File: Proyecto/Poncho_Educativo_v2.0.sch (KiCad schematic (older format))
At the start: 0 parts

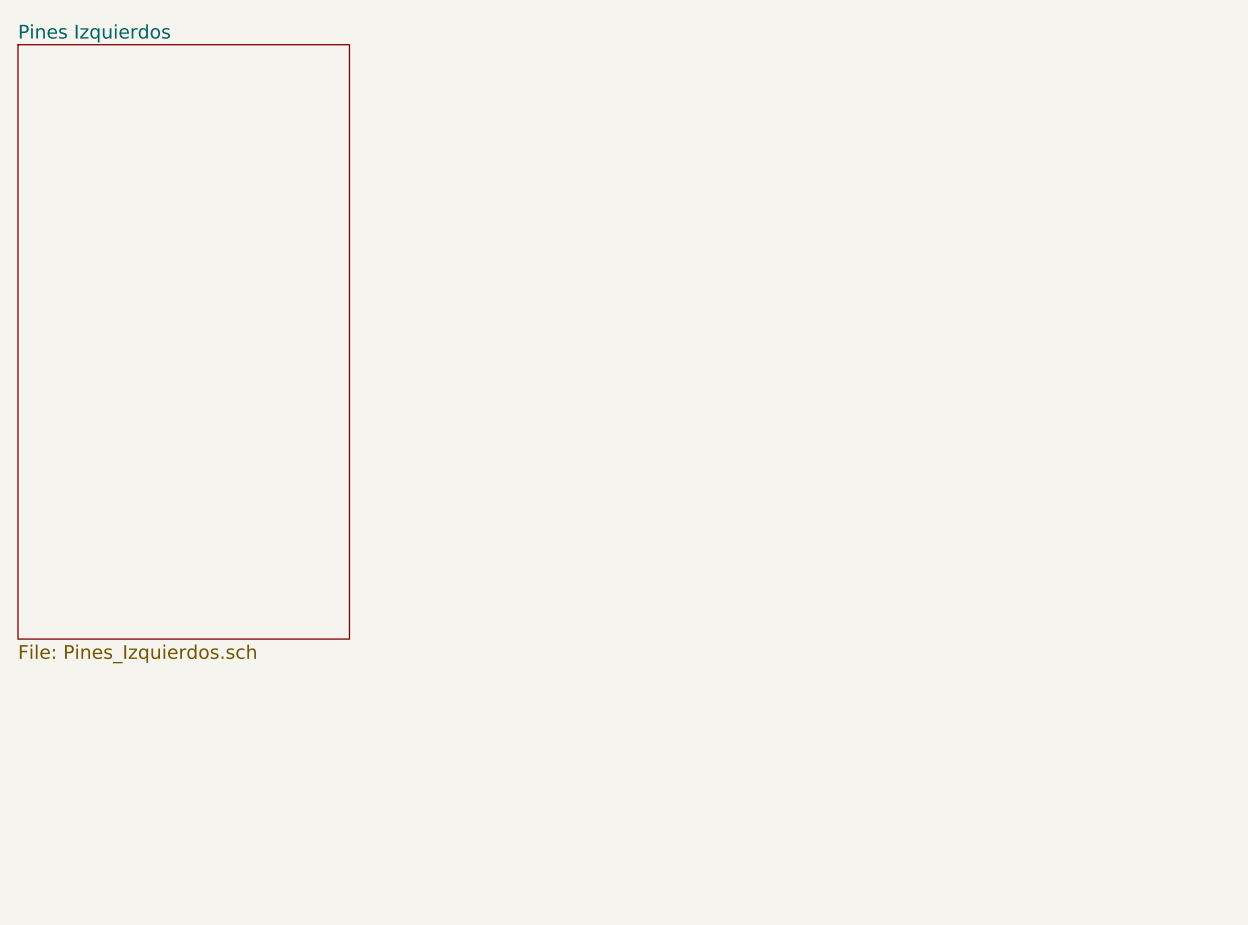
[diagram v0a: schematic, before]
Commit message: Actualización de documentación y esquemáticos.
Se actualizaron los archivos de datos y caracteristicas de los displays
y se adelantó a un 90% el diseño de los esquemáticos de KiCad.
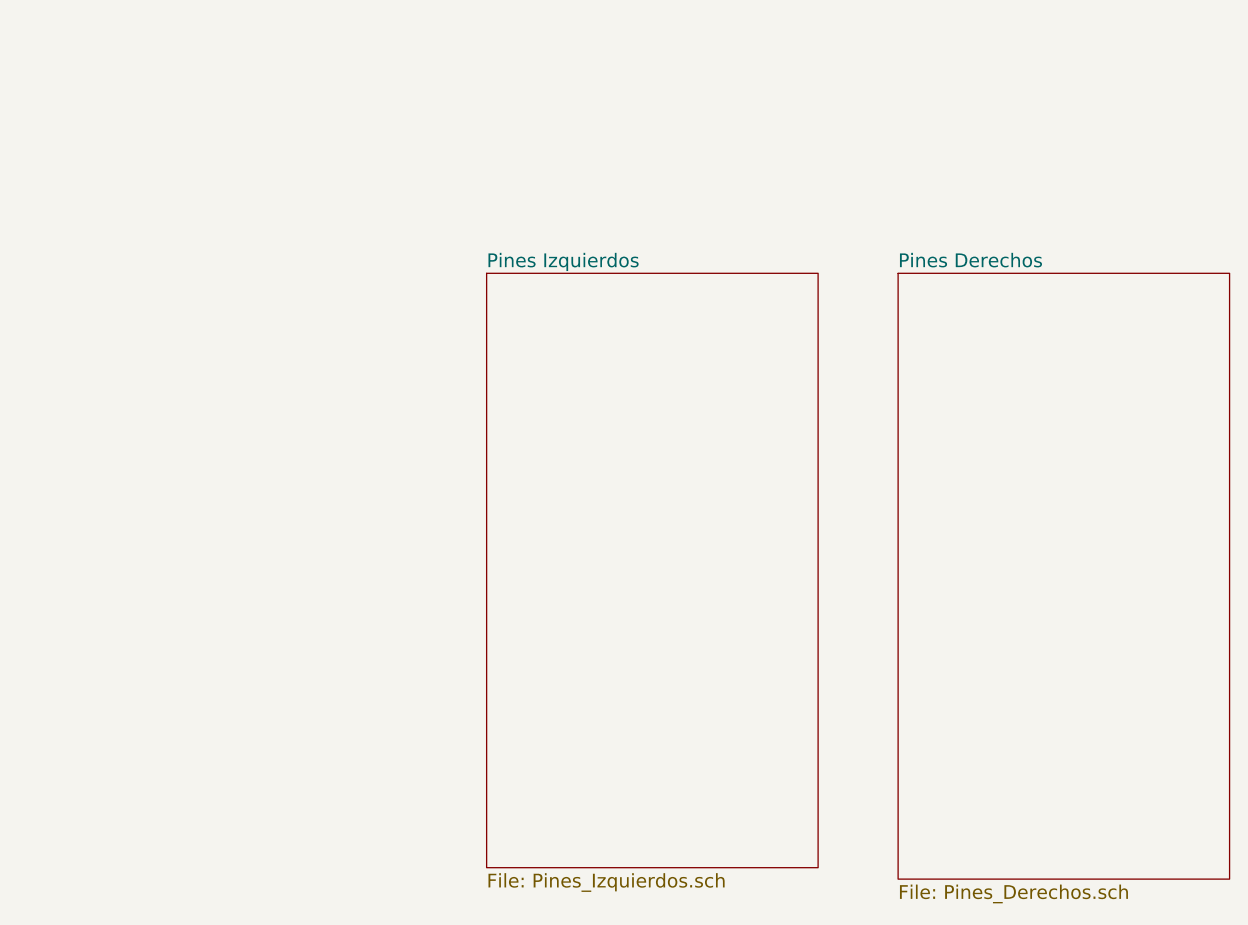
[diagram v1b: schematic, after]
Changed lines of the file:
@@
 EESchema Schematic File Version 2
+LIBS:8x8led-cache
 LIBS:power
 LIBS:device
 LIBS:display
+LIBS:Poncho_Esqueleto
+LIBS:MAX7219
 LIBS:Poncho_Educativo_v2.0-cache
 EELAYER 25 0
@@
 $Descr A4 11693 8268
 encoding utf-8
-Sheet 1 2
+Sheet 1 3
 Title "Poncho Educativo v2.0"
 Date "2017-05-15"
@@
 $EndDescr
 $Sheet
-S 1250 1150 1450 2600
+S 3300 2150 1450 2600
 U 591BB8C8
 F0 "Pines Izquierdos" 60
 F1 "Pines_Izquierdos.sch" 60
 $EndSheet
+$Sheet
+S 5100 2150 1450 2650
+U 5926FB74
+F0 "Pines Derechos" 60
+F1 "Pines_Derechos.sch" 60
+$EndSheet
 $EndSCHEMATC

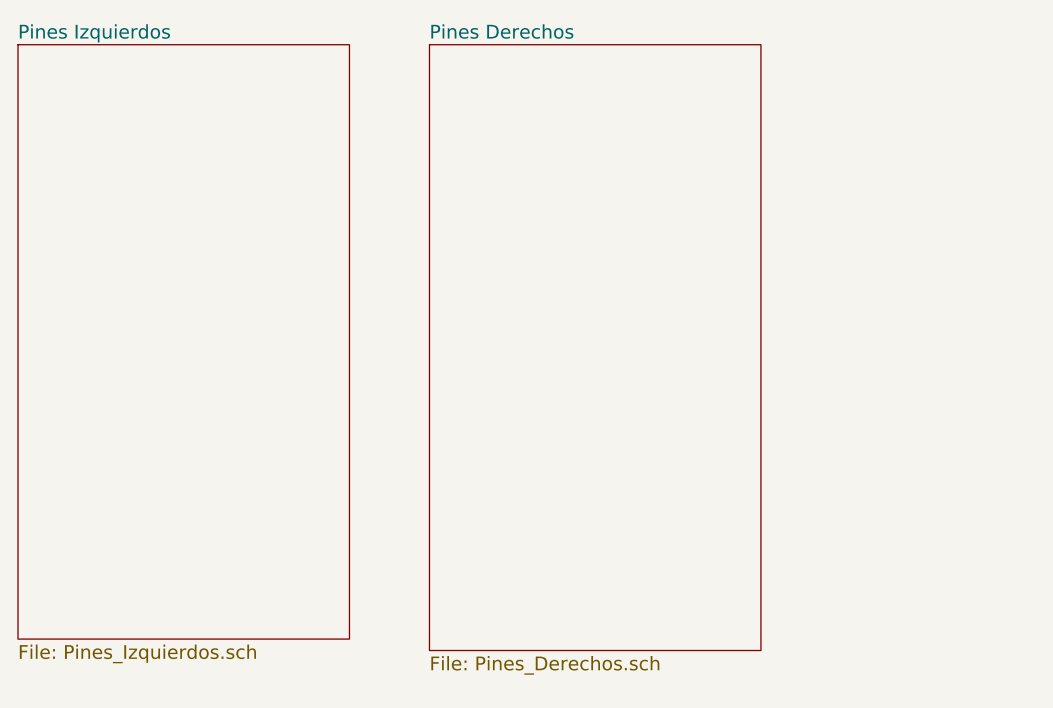
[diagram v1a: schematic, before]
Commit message: Avance de FootPrints
Se terminó diseño de esquemáticos en ojas Jerárquicas; se avanzó a un
70% en las referencias de FootPrint, y se actualizaron hojas de datos de
la Matriz de LEDs 8x8.
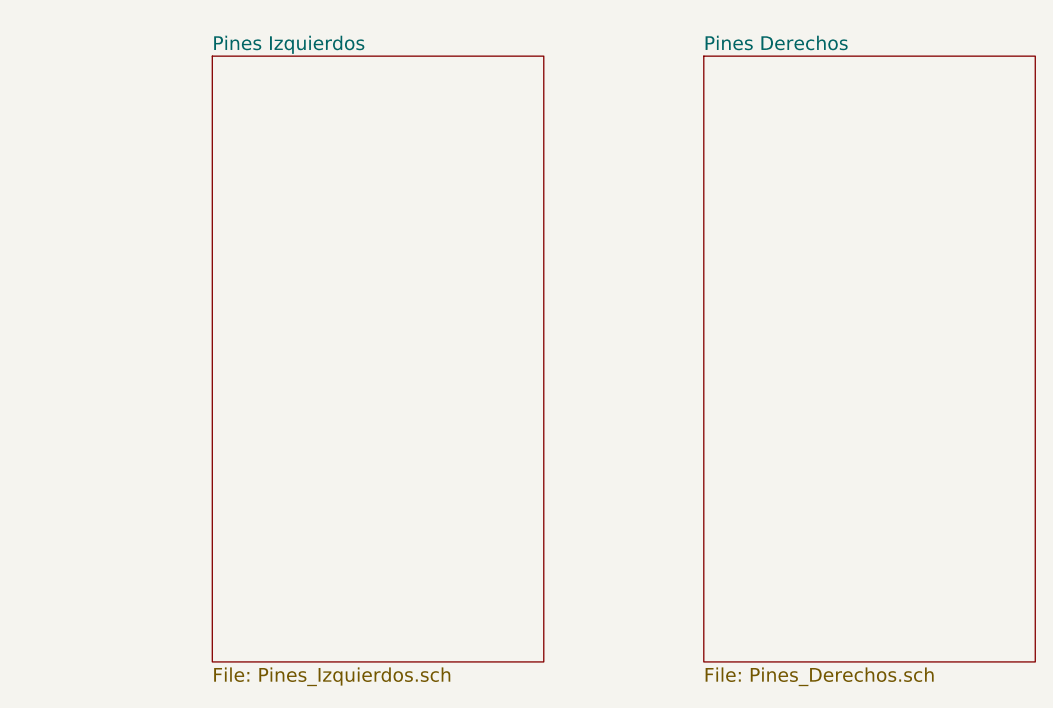
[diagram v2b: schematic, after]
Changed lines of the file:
@@
 EESchema Schematic File Version 2
-LIBS:8x8led-cache
 LIBS:power
 LIBS:device
 LIBS:display
 LIBS:Poncho_Esqueleto
-LIBS:MAX7219
 LIBS:Poncho_Educativo_v2.0-cache
 EELAYER 25 0
@@
 $EndDescr
 $Sheet
-S 3300 2150 1450 2600
+S 6300 2200 1450 2650
+U 5926FB74
+F0 "Pines Derechos" 60
+F1 "Pines_Derechos.sch" 60
+$EndSheet
+$Sheet
+S 4150 2200 1450 2650
 U 591BB8C8
 F0 "Pines Izquierdos" 60
 F1 "Pines_Izquierdos.sch" 60
 $EndSheet
-$Sheet
-S 5100 2150 1450 2650
-U 5926FB74
-F0 "Pines Derechos" 60
-F1 "Pines_Derechos.sch" 60
-$EndSheet
 $EndSCHEMATC

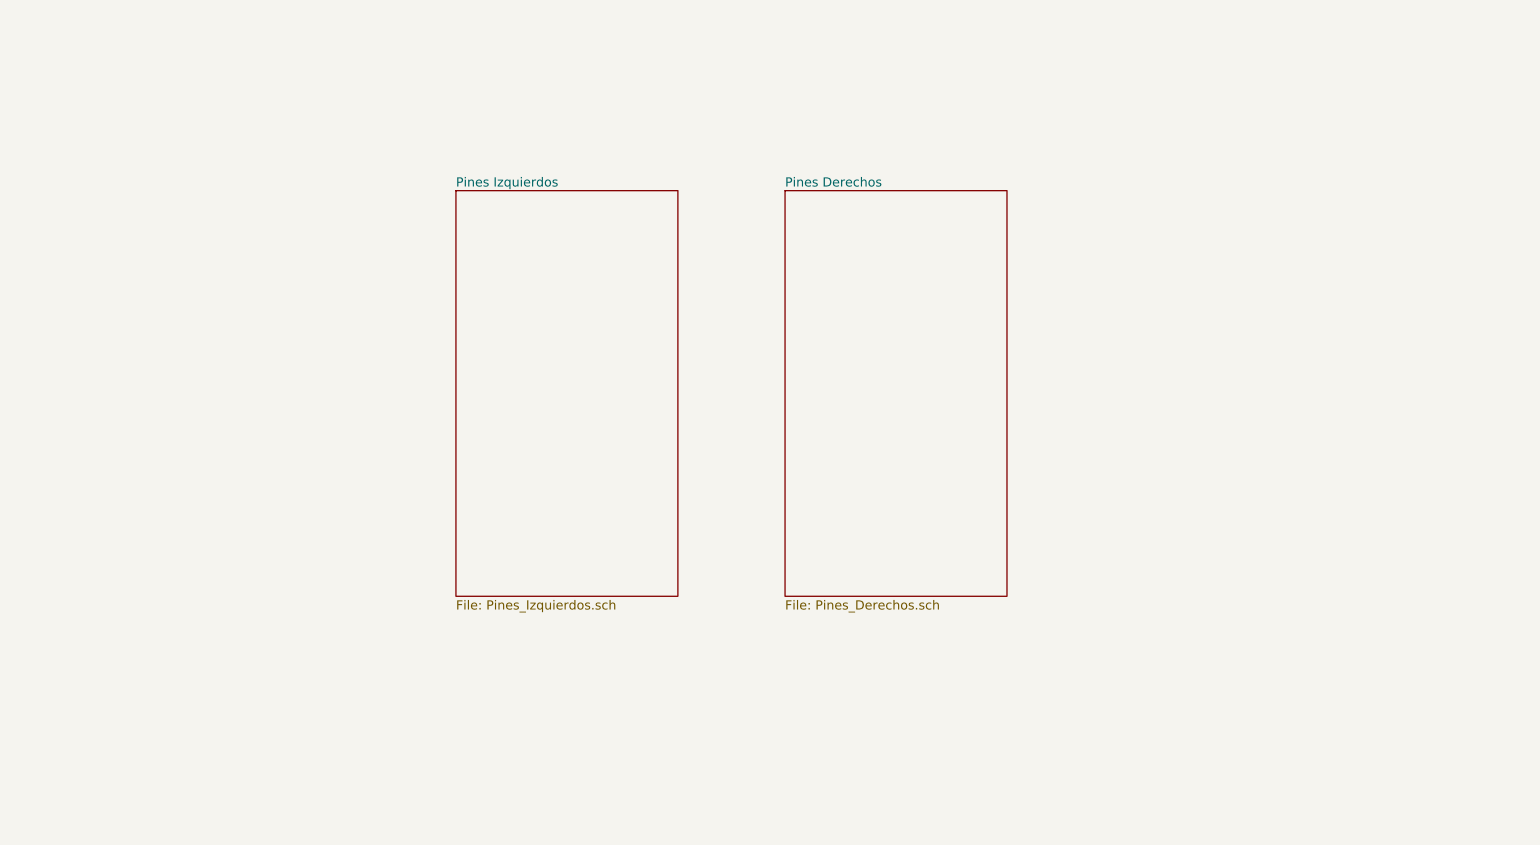
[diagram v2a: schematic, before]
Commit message: Modelos 3D
Se modificaron FootPrints y se agregaron modelos en 3D.
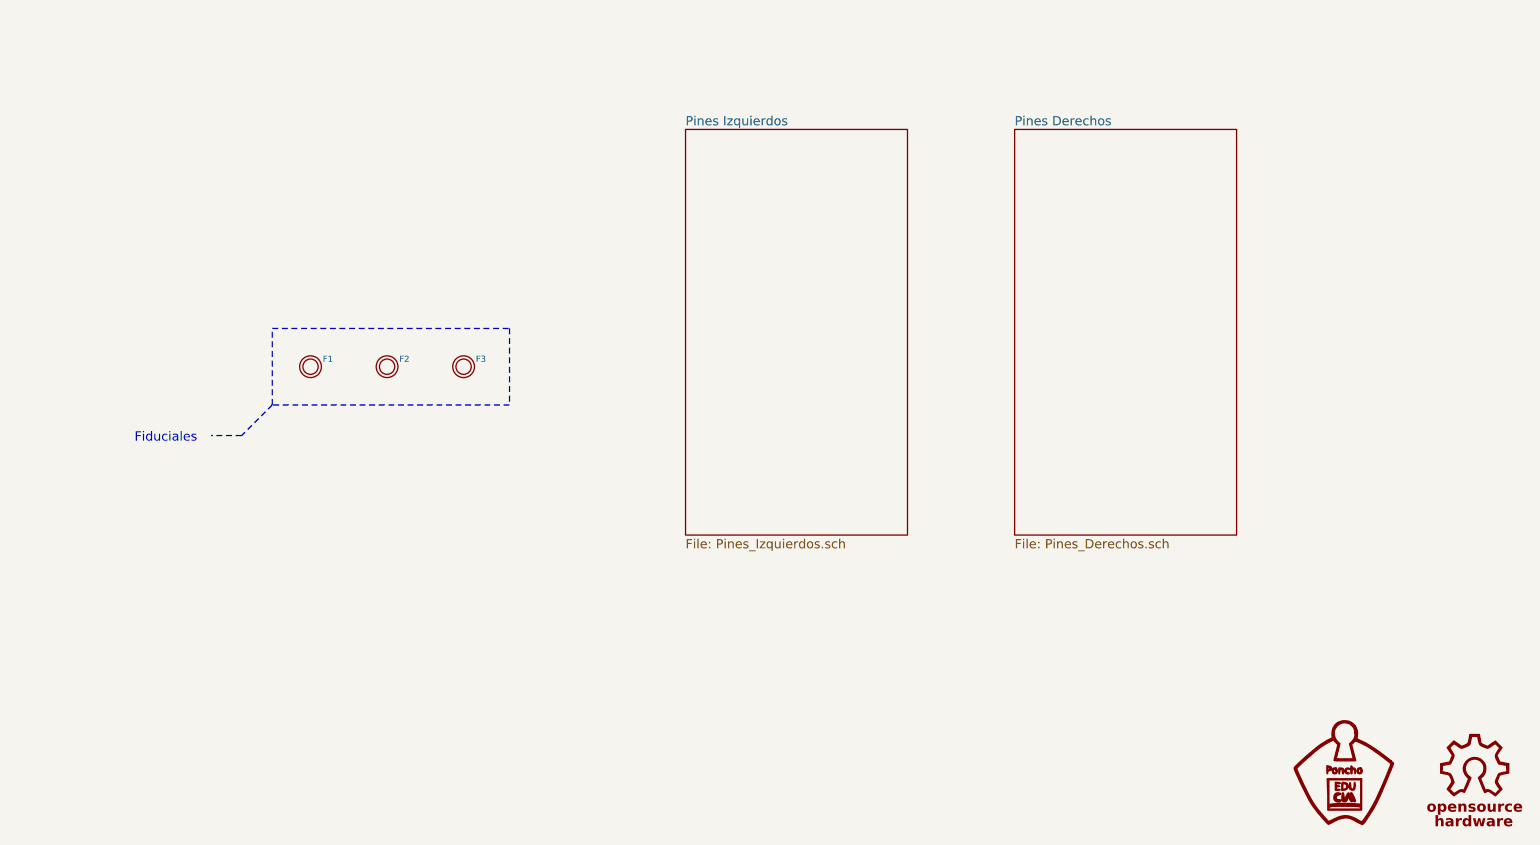
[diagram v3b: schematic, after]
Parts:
- added F1, F2, F3: FIDUCIAL, FootPrints:Fiducial_1mm, symbol FIDUCIAL
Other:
- note added: "Fiduciales"
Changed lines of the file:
@@
 $EndDescr
 $Sheet
-S 6300 2200 1450 2650
+S 7800 1800 1450 2650
 U 5926FB74
 F0 "Pines Derechos" 60
@@
 $EndSheet
 $Sheet
-S 4150 2200 1450 2650
+S 5650 1800 1450 2650
 U 591BB8C8
 F0 "Pines Izquierdos" 60
 F1 "Pines_Izquierdos.sch" 60
 $EndSheet
+$Comp
+L FIDUCIAL F1
+U 1 1 592B6856
+P 3200 3350
+F 0 "F1" H 3280 3400 40  0000 L CNN
+F 1 "FIDUCIAL" H 3200 3250 30  0001 C CNN
+F 2 "FootPrints:Fiducial_1mm" H 3200 3400 60  0001 C CNN
+F 3 "" H 3200 3400 60  0001 C CNN
+F 4 "FIDUCIAL" H 3250 3150 60  0001 C CNN "Descripcion"
+	1    3200 3350
+	1    0    0    -1
+$EndComp
+$Comp
+L FIDUCIAL F2
+U 1 1 592B68A6
+P 3700 3350
+F 0 "F2" H 3780 3400 40  0000 L CNN
+F 1 "FIDUCIAL" H 3700 3250 30  0001 C CNN
+F 2 "FootPrints:Fiducial_1mm" H 3700 3400 60  0001 C CNN
+F 3 "" H 3700 3400 60  0001 C CNN
+F 4 "FIDUCIAL" H 3750 3150 60  0001 C CNN "Descripcion"
+	1    3700 3350
+	1    0    0    -1
+$EndComp
+$Comp
+L FIDUCIAL F3
+U 1 1 592B68FC
+P 4200 3350
+F 0 "F3" H 4280 3400 40  0000 L CNN
+F 1 "FIDUCIAL" H 4200 3250 30  0001 C CNN
+F 2 "FootPrints:Fiducial_1mm" H 4200 3400 60  0001 C CNN
+F 3 "" H 4200 3400 60  0001 C CNN
+F 4 "FIDUCIAL" H 4250 3150 60  0001 C CNN "Descripcion"
+	1    4200 3350
+	1    0    0    -1
+$EndComp
+Text Notes 2050 3850 0    60   ~ 0
+Fiduciales
+Wire Notes Line
+	2950 3100 4500 3100
+Wire Notes Line
+	4500 3100 4500 3600
+Wire Notes Line
+	4500 3600 2950 3600
+Wire Notes Line
+	2950 3600 2950 3100
+Wire Notes Line
+	2950 3600 2750 3800
+Wire Notes Line
+	2750 3800 2550 3800
+$Comp
+L Logo_Poncho #G1
+U 1 1 5934255D
+P 9950 6000
+F 0 "#G1" H 9900 5600 60  0001 C CNN
+F 1 "Logo_Poncho" H 10150 5600 60  0001 C CNN
+F 2 "" H 9950 6000 60  0000 C CNN
+F 3 "" H 9950 6000 60  0000 C CNN
+	1    9950 6000
+	1    0    0    -1
+$EndComp
+$Comp
+L OSHWA #G2
+U 1 1 59342577
+P 10800 6050
+F 0 "#G2" H 10770 6450 60  0001 C CNN
+F 1 "OSHWA" H 10800 6353 60  0001 C CNN
+F 2 "" H 10800 6050 60  0000 C CNN
+F 3 "" H 10800 6050 60  0000 C CNN
+	1    10800 6050
+	1    0    0    -1
+$EndComp
 $EndSCHEMATC
